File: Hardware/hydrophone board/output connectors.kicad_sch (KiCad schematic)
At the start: 2 parts

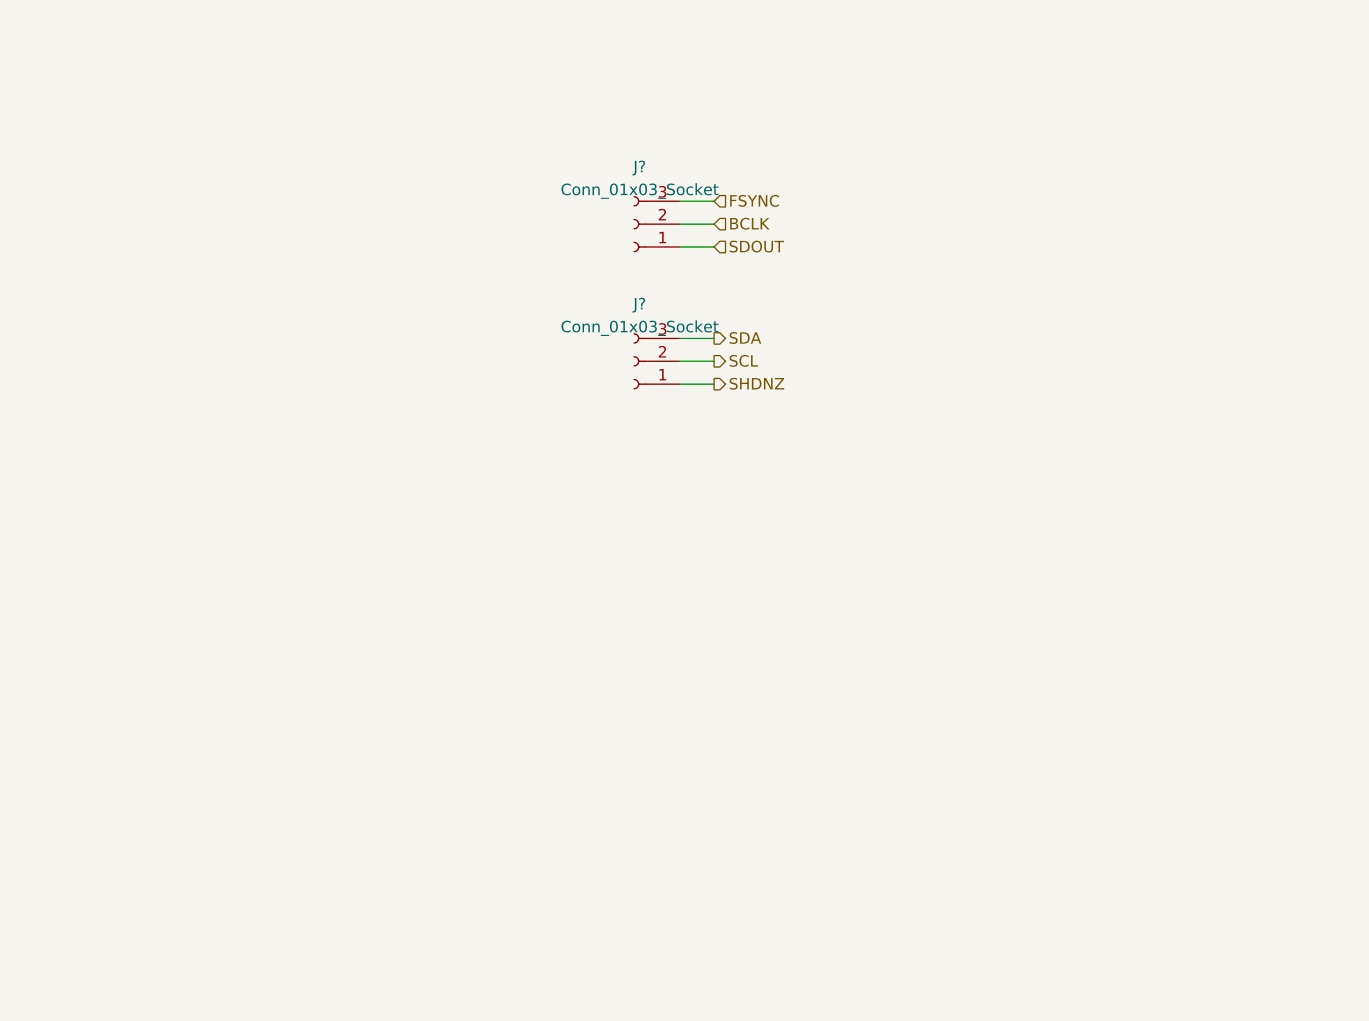
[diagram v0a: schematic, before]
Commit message: added teensy footprint
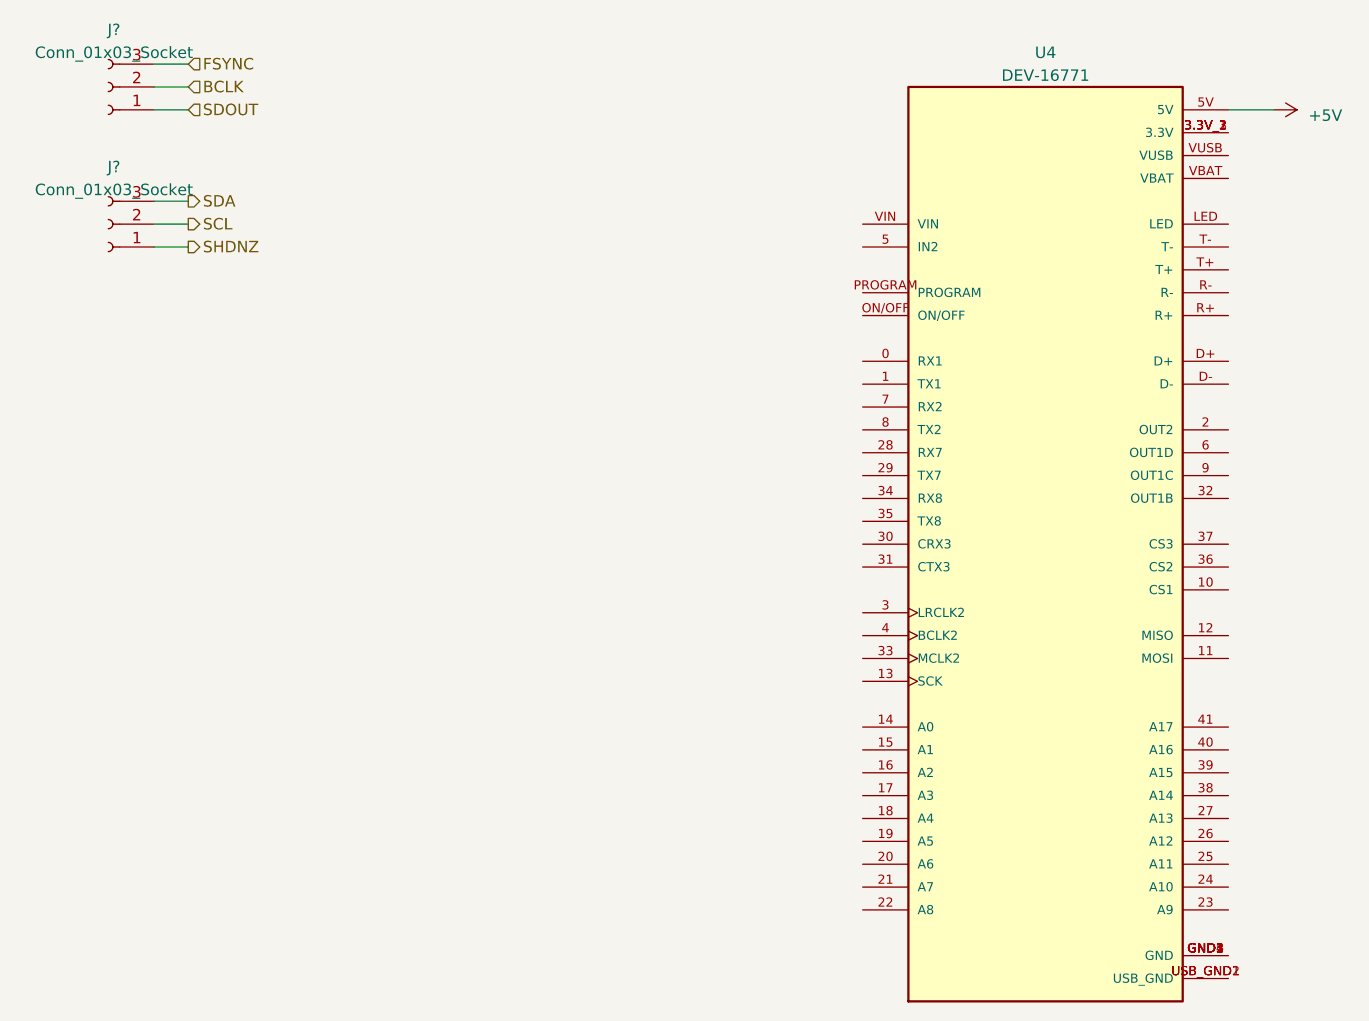
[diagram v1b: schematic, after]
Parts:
- added U4: DEV-16771, DEV-16771:MODULE_DEV-16771, symbol DEV-16771:DEV-16771
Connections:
- new net: U4.3.3V_1 (3.3V), U4.3.3V_2 (3.3V), U4.3.3V_3 (3.3V)
- new net: U4.GND1 (GND), U4.GND2 (GND), U4.GND3 (GND), U4.GND4 (GND), U4.GND5 (GND)
- new net: U4.USB_GND1 (USB_GND), U4.USB_GND2 (USB_GND)
- new net +5V: U4.5V
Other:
- moved on the sheet: J?
